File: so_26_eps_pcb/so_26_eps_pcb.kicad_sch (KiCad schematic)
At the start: 83 parts, among them J1 Conn_02x12_Odd_Even, SW1 SW_SPDT

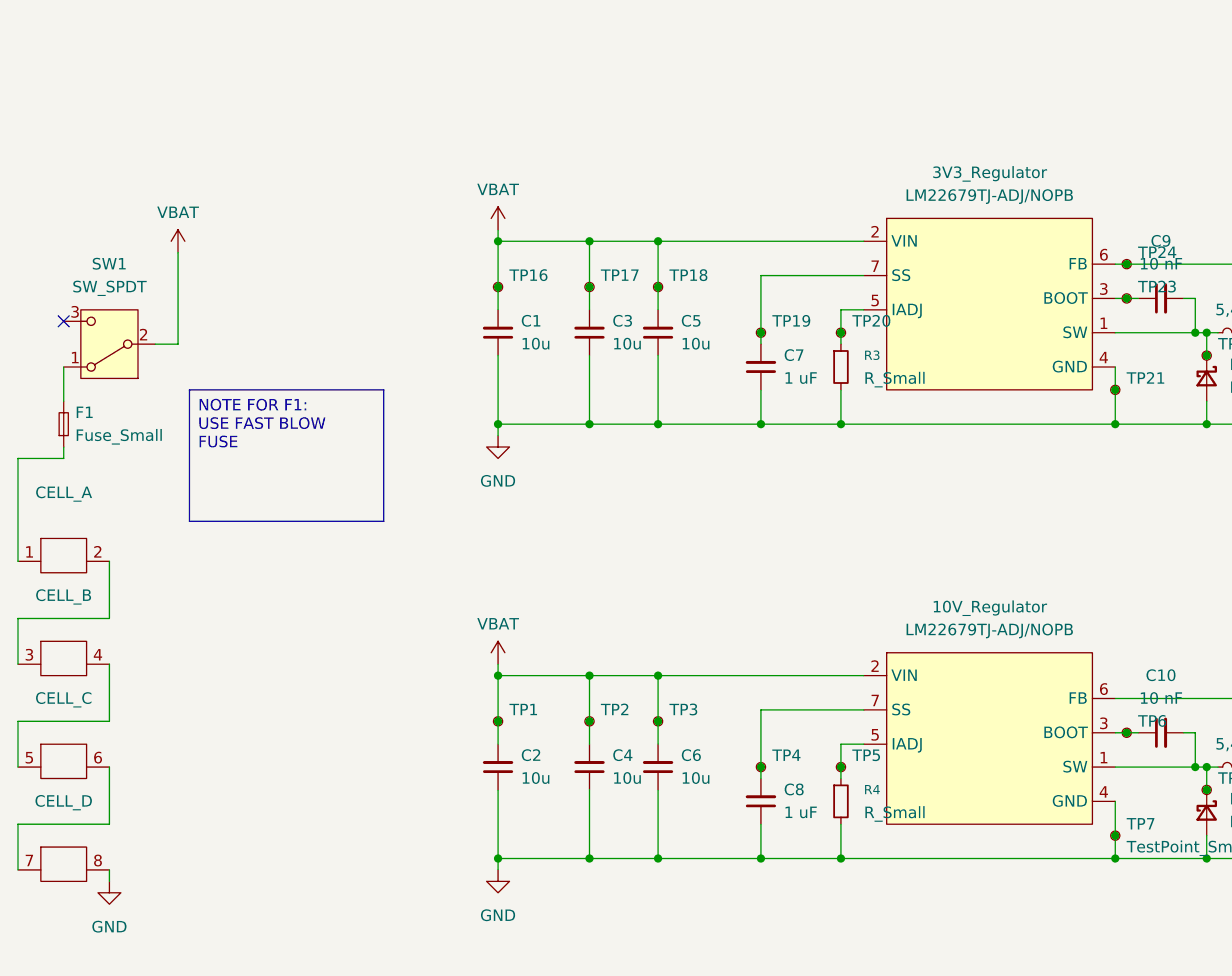
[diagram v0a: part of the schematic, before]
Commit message: Made battery holder footprint
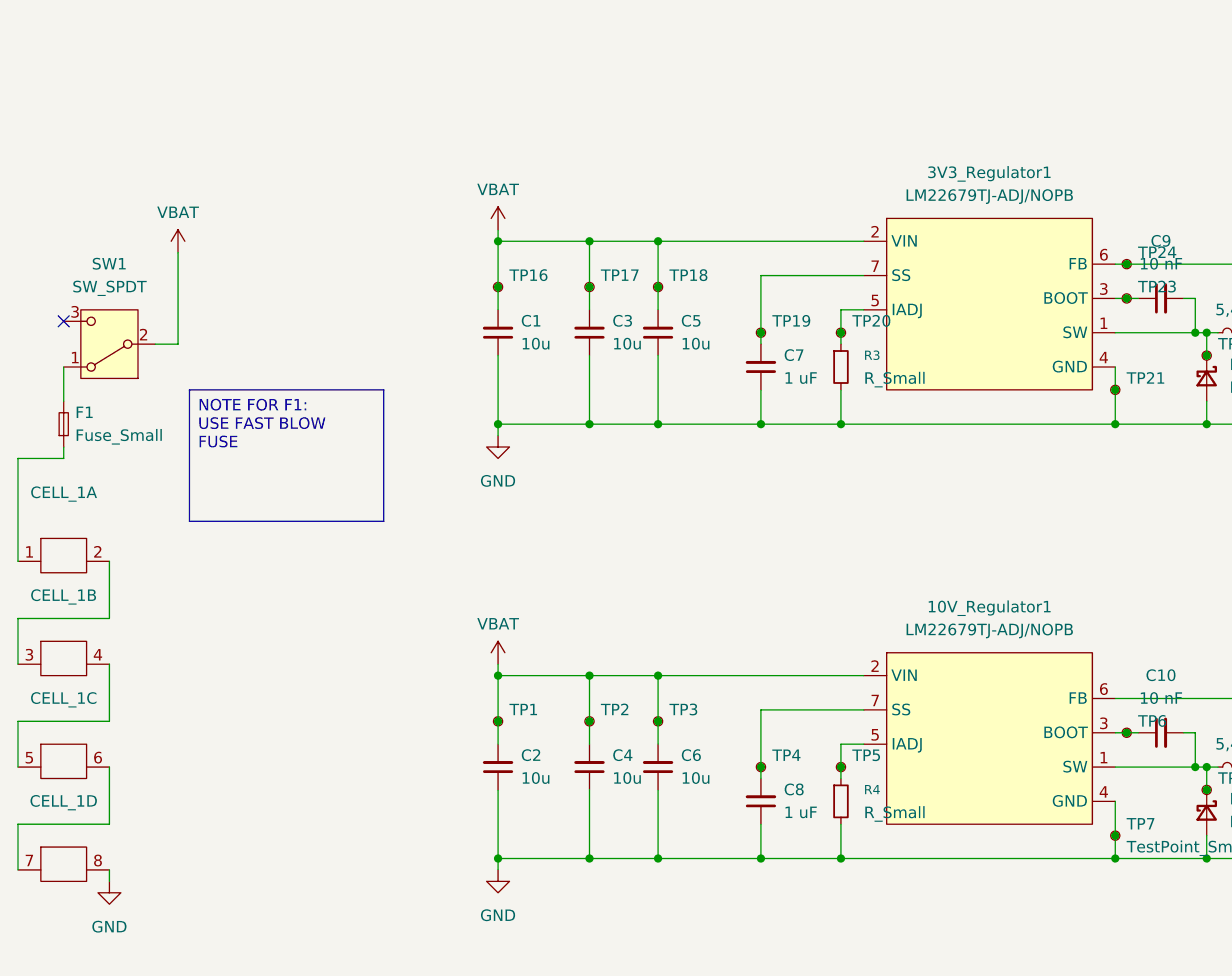
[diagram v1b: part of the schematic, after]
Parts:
- CELL_1: renamed from CELL_; footprint (none) -> Myfootprints:Battery holder
- renumbered 10V_Regulator to 10V_Regulator1, 3V3_Regulator to 3V3_Regulator1
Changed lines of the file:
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@@
 		(dnp no)
 		(fields_autoplaced yes)
-		(property "Reference" "CELL_"
+		(property "Reference" "CELL_1"
 			(at 27.94 105.41 0)
 			(effects
@@
 			)
 		)
-		(property "Footprint" ""
+		(property "Footprint" "Myfootprints:Battery holder"
 			(at 27.94 109.22 0)
 			(effects
@@
 			(project ""
 				(path "/bf42000f-dc59-47af-ab4a-8f583481d44f"
-					(reference "CELL_")
+					(reference "CELL_1")
 					(unit 4)
 				)
@@
 		(dnp no)
 		(fields_autoplaced yes)
-		(property "Reference" "CELL_"
+		(property "Reference" "CELL_1"
 			(at 27.94 93.98 0)
 			(effects
@@
 			)
 		)
-		(property "Footprint" ""
+		(property "Footprint" "Myfootprints:Battery holder"
 			(at 27.94 97.79 0)
 			(effects
@@
 			(project ""
 				(path "/bf42000f-dc59-47af-ab4a-8f583481d44f"
-					(reference "CELL_")
+					(reference "CELL_1")
 					(unit 3)
 				)
@@
 		(dnp no)
 		(fields_autoplaced yes)
-		(property "Reference" "3V3_Regulator"
+		(property "Reference" "3V3_Regulator1"
 			(at 130.81 35.56 0)
 			(effects
@@
 			(project ""
 				(path "/bf42000f-dc59-47af-ab4a-8f583481d44f"
-					(reference "3V3_Regulator")
+					(reference "3V3_Regulator1")
 					(unit 1)
 				)
@@
 		(dnp no)
 		(fields_autoplaced yes)
-		(property "Reference" "CELL_"
+		(property "Reference" "CELL_1"
 			(at 27.94 71.12 0)
 			(effects
@@
 			)
 		)
-		(property "Footprint" ""
+		(property "Footprint" "Myfootprints:Battery holder"
 			(at 27.94 73.66 0)
 			(effects
@@
 			(project ""
 				(path "/bf42000f-dc59-47af-ab4a-8f583481d44f"
-					(reference "CELL_")
+					(reference "CELL_1")
 					(unit 1)
 				)
@@
 		(dnp no)
 		(fields_autoplaced yes)
-		(property "Reference" "10V_Regulator"
+		(property "Reference" "10V_Regulator1"
 			(at 130.81 83.82 0)
 			(effects
@@
 			(project "so_26_eps_pcb"
 				(path "/bf42000f-dc59-47af-ab4a-8f583481d44f"
-					(reference "10V_Regulator")
+					(reference "10V_Regulator1")
 					(unit 1)
 				)
@@
 		(dnp no)
 		(fields_autoplaced yes)
-		(property "Reference" "CELL_"
+		(property "Reference" "CELL_1"
 			(at 27.94 82.55 0)
 			(effects
@@
 			)
 		)
-		(property "Footprint" ""
+		(property "Footprint" "Myfootprints:Battery holder"
 			(at 27.94 86.36 0)
 			(effects
@@
 			(project ""
 				(path "/bf42000f-dc59-47af-ab4a-8f583481d44f"
-					(reference "CELL_")
+					(reference "CELL_1")
 					(unit 2)
 				)

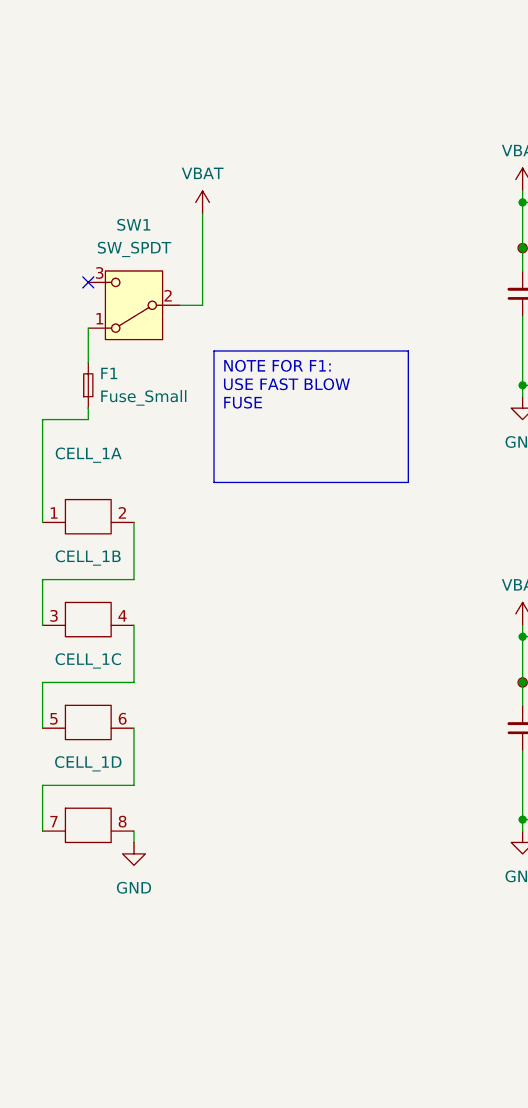
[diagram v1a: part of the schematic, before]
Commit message: Added the last footprints
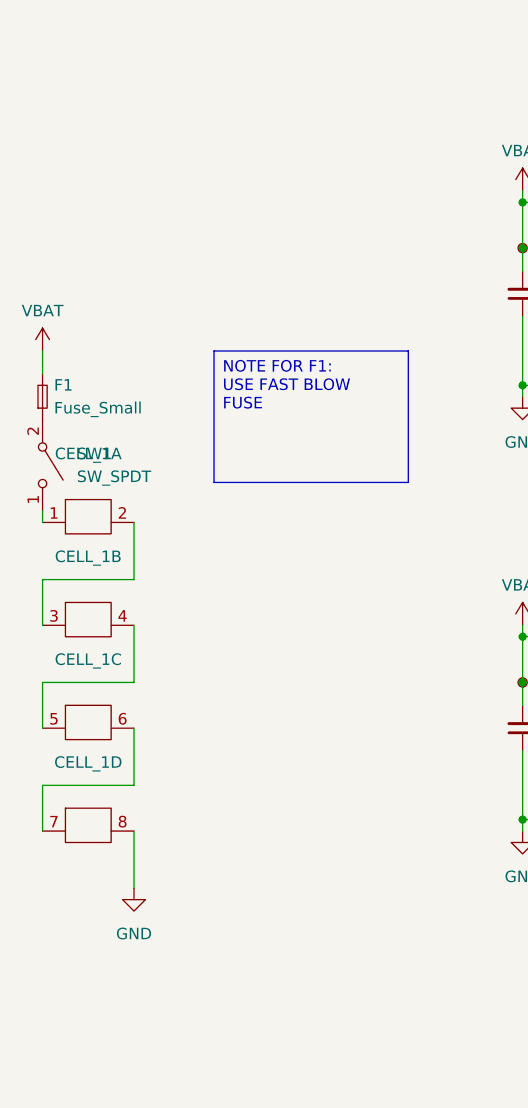
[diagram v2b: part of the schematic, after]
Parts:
- D1, D2, D3: footprint (none) -> Diode_SMD:D_SOD-128
- F1: footprint (none) -> Myfootprints:Surface Mount Fuse Block
- L1, L2: footprint (none) -> Myfootprints:SRU1048 Inductor
- SW1: footprint (none) -> Connector_PinSocket_2.54mm:PinSocket_1x02_P2.54mm_Vertical
- TP1, TP10, TP11, TP12, TP13, TP14, TP15, TP16, TP17, TP18, TP19, TP2, TP20, TP21, TP22, TP23, TP24, TP25, TP26, TP27, TP28, TP29, TP3, TP30, TP31, TP32, TP33, TP34, TP35, TP36, TP37, TP4, TP5, TP6, TP7, TP8, TP9: footprint TestPoint:TestPoint_Pad_D2.5mm -> TestPoint:TestPoint_Pad_D2.0mm
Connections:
- net VBAT: now also F1.2; no longer SW1.2 (B)
- net at SW1.1 (A): now also CELL_1.1; no longer F1.2
- net at F1.1: now also SW1.2 (B); no longer CELL_1.1
- no-connect marks 1 -> 0
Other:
- moved on the sheet: F1
